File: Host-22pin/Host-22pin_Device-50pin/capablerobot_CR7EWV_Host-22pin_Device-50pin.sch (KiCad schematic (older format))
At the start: 2 parts, among them J1 WE_687622100002_FLEX, J2 WE_687650100002_FLEX

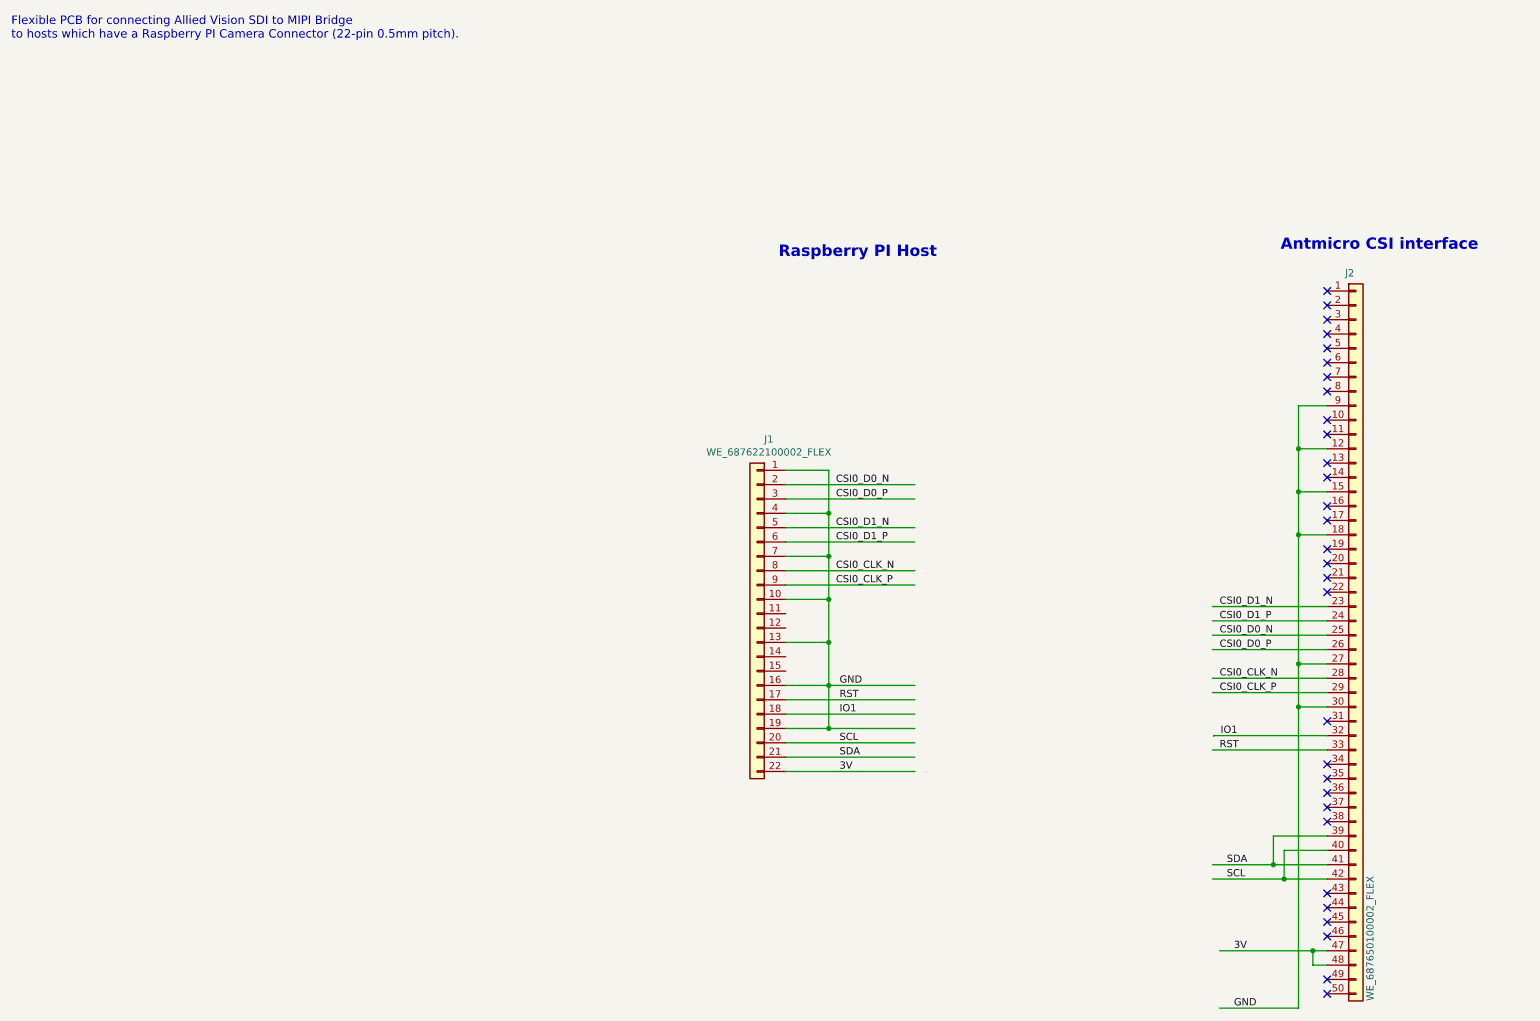
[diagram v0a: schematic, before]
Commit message: Change 22 pin to 4 lane interface and change 15 pin and 22 pin to alternate MIPI interface
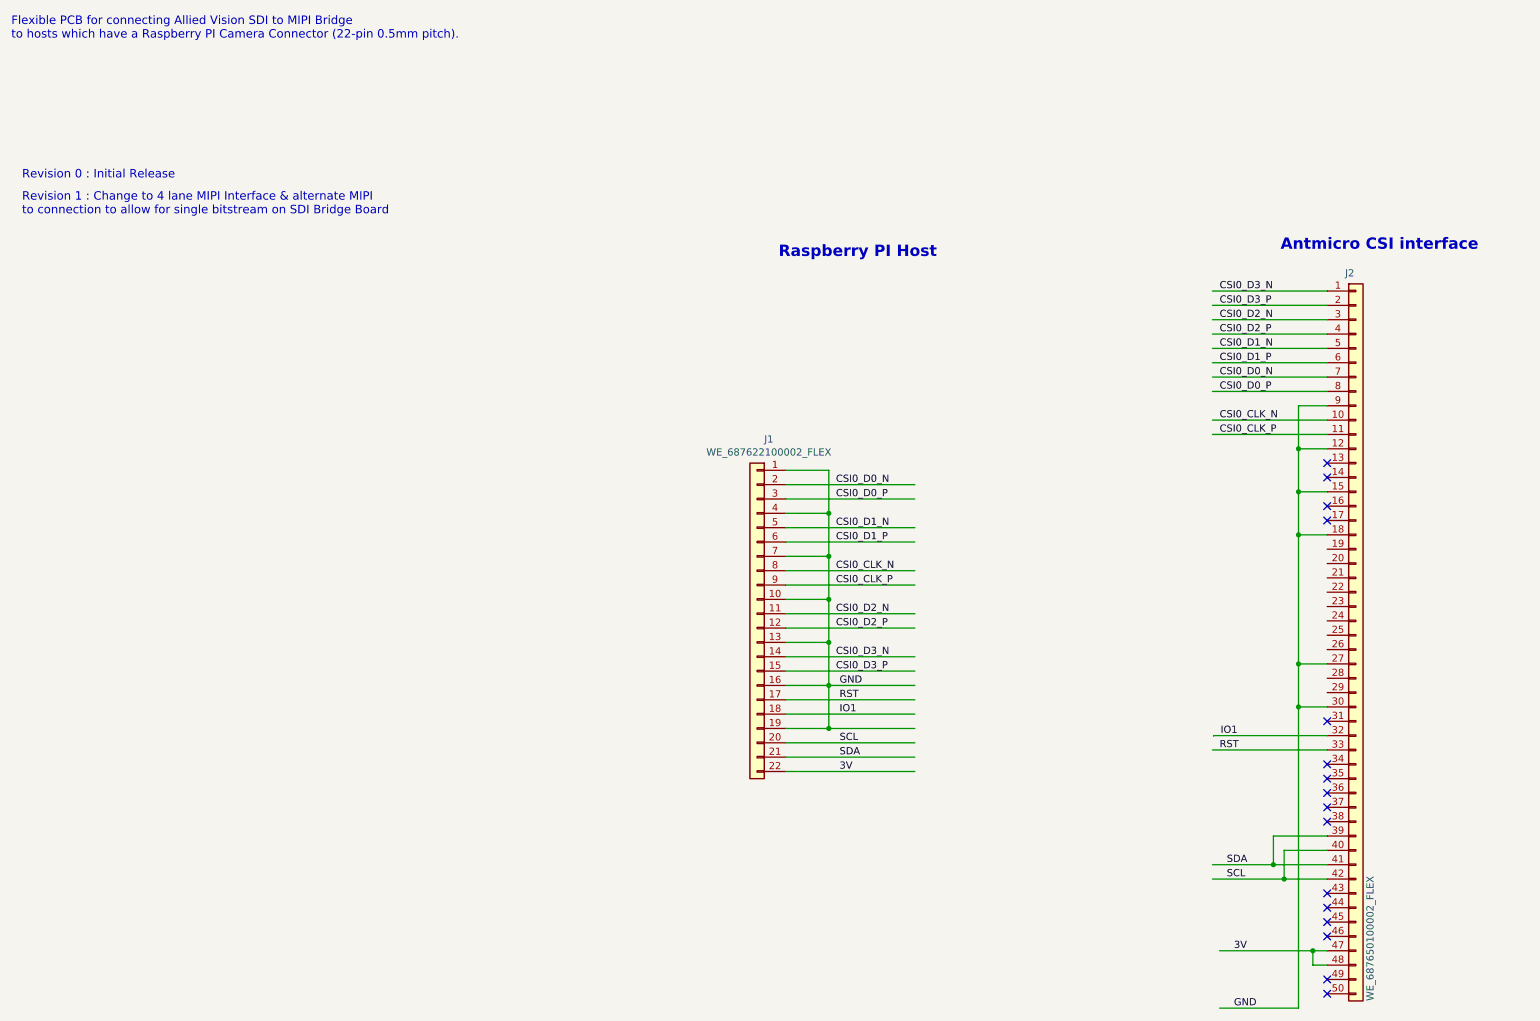
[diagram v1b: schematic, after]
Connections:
- net labels added: CSI0_D2_N, CSI0_D2_P, CSI0_D3_N, CSI0_D3_P
- wire segments 60 -> 68
- no-connect marks 30 -> 16
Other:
- note added: "Revision 0 : Initial Release"
- note added: "Revision 1 : Change to 4 lane MIPI Interface & alternate MIPI\nto connection to allow for single bitstream on SDI Bridge Board"
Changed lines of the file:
@@
 NoConn ~ 10100 6575
 NoConn ~ 10100 6275
-NoConn ~ 10100 3275
-NoConn ~ 10100 3375
-NoConn ~ 10100 3475
-NoConn ~ 10100 3575
-NoConn ~ 10100 3675
-NoConn ~ 10100 3775
-NoConn ~ 10100 3875
-NoConn ~ 10100 3975
-NoConn ~ 10100 4175
-NoConn ~ 10100 4275
 NoConn ~ 10100 4475
 NoConn ~ 10100 4575
@@
 Text Label 9400 7375 0    50   ~ 0
 SCL
-Text Label 9350 5475 0    50   ~ 0
-CSI0_D1_N
-Text Label 9350 5575 0    50   ~ 0
-CSI0_D1_P
-Text Label 9350 5675 0    50   ~ 0
-CSI0_D0_N
-Text Label 9350 5775 0    50   ~ 0
-CSI0_D0_P
-Text Label 9350 5975 0    50   ~ 0
-CSI0_CLK_N
-Text Label 9350 6075 0    50   ~ 0
-CSI0_CLK_P
-Wire Wire Line
-	10100 6075 9300 6075
-Wire Wire Line
-	10100 5975 9300 5975
-Wire Wire Line
-	10100 5775 9300 5775
-Wire Wire Line
-	10100 5675 9300 5675
-Wire Wire Line
-	10100 5575 9300 5575
-Wire Wire Line
-	10100 5475 9300 5475
 Wire Wire Line
 	10100 7375 9800 7375
@@
 Wire Wire Line
 	10100 4075 9900 4075
-$Comp
-L antmicro-alvium-flex-csi-adapter:WE_687650100002_FLEX J2
-U 1 1 5FE0645A
-P 10300 4875
-F 0 "J2" H 10225 6600 50  0000 L CNN
-F 1 "WE_687650100002_FLEX" V 10400 1525 50  0000 L CNN
-F 2 "antmicro-alvium-flex-csi-adapter-footprints:WE_687650100002_FLEX" H 10100 1325 50  0001 C CNN
-F 3 "" H 10300 1225 50  0001 C CNN
-F 4 "687650100002" H 10700 4275 60  0001 L CNN "MPN"
-F 5 "Wurth Elektronik " H 10950 3075 60  0001 L CNN "Manufacturer"
-	1    10300 4875
-	1    0    0    -1
-$EndComp
 $Bitmap
 Pos 3200 10650
@@
 	6625 4525 6625 4825
 Connection ~ 6625 4825
-NoConn ~ 10100 5375
-NoConn ~ 10100 5275
-NoConn ~ 10100 5175
-NoConn ~ 10100 5075
 Wire Wire Line
 	10100 6375 9308 6375
@@
 Wire Wire Line
 	6325 6025 6625 6025
+Wire Wire Line
+	6325 5525 7225 5525
+Wire Wire Line
+	6325 5625 7225 5625
+Wire Wire Line
+	6325 5825 7225 5825
+Wire Wire Line
+	6325 5925 7225 5925
+Text Label 6675 5525 0    50   ~ 0
+CSI0_D2_N
+Text Label 6675 5625 0    50   ~ 0
+CSI0_D2_P
+Text Label 6675 5825 0    50   ~ 0
+CSI0_D3_N
+Text Label 6675 5925 0    50   ~ 0
+CSI0_D3_P
+$Comp
+L antmicro-alvium-flex-csi-adapter:WE_687650100002_FLEX J2
+U 1 1 5FE0645A
+P 10300 4875
+F 0 "J2" H 10225 6600 50  0000 L CNN
+F 1 "WE_687650100002_FLEX" V 10400 1525 50  0000 L CNN
+F 2 "antmicro-alvium-flex-csi-adapter-footprints:WE_687650100002_FLEX" H 10100 1325 50  0001 C CNN
+F 3 "" H 10300 1225 50  0001 C CNN
+F 4 "687650100002" H 10700 4275 60  0001 L CNN "MPN"
+F 5 "Wurth Elektronik " H 10950 3075 60  0001 L CNN "Manufacturer"
+	1    10300 4875
+	1    0    0    -1
+$EndComp
+Wire Wire Line
+	10100 3275 9300 3275
+Wire Wire Line
+	10100 3375 9300 3375
+Wire Wire Line
+	10100 3475 9300 3475
+Wire Wire Line
+	10100 3575 9300 3575
+Wire Wire Line
+	10100 3675 9300 3675
+Wire Wire Line
+	10100 3775 9300 3775
+Wire Wire Line
+	10100 3875 9300 3875
+Wire Wire Line
+	10100 3975 9300 3975
+Wire Wire Line
+	10100 4175 9300 4175
+Wire Wire Line
+	10100 4275 9300 4275
+Text Label 9350 4275 0    50   ~ 0
+CSI0_CLK_P
+Text Label 9350 4175 0    50   ~ 0
+CSI0_CLK_N
+Text Label 9350 3975 0    50   ~ 0
+CSI0_D0_P
+Text Label 9350 3875 0    50   ~ 0
+CSI0_D0_N
+Text Label 9350 3775 0    50   ~ 0
+CSI0_D1_P
+Text Label 9350 3675 0    50   ~ 0
+CSI0_D1_N
+Text Label 9350 3575 0    50   ~ 0
+CSI0_D2_P
+Text Label 9350 3475 0    50   ~ 0
+CSI0_D2_N
+Text Label 9350 3375 0    50   ~ 0
+CSI0_D3_P
+Text Label 9350 3275 0    50   ~ 0
+CSI0_D3_N
+Text Notes 1000 2500 0    59   ~ 0
+Revision 0 : Initial Release
+Text Notes 1000 2750 0    59   ~ 0
+Revision 1 : Change to 4 lane MIPI Interface & alternate MIPI\nto connection to allow for single bitstream on SDI Bridge Board
 $EndSCHEMATC
